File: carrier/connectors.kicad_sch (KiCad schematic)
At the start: 2 parts, among them J11 2199119-8, J12 Conn_01x05

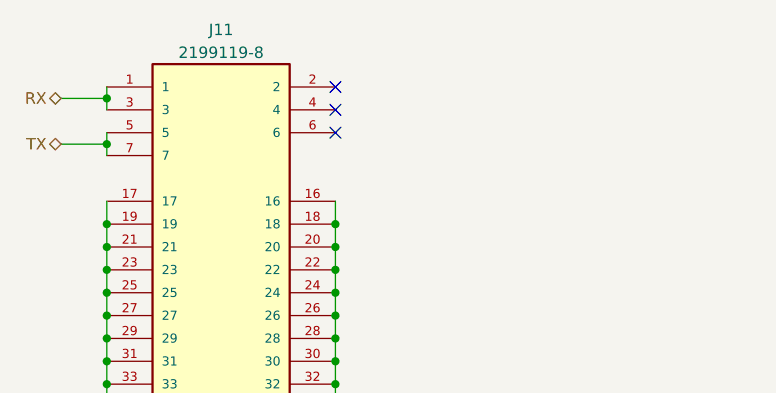
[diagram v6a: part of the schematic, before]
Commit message: Feat: most routes on i2c side and power complete
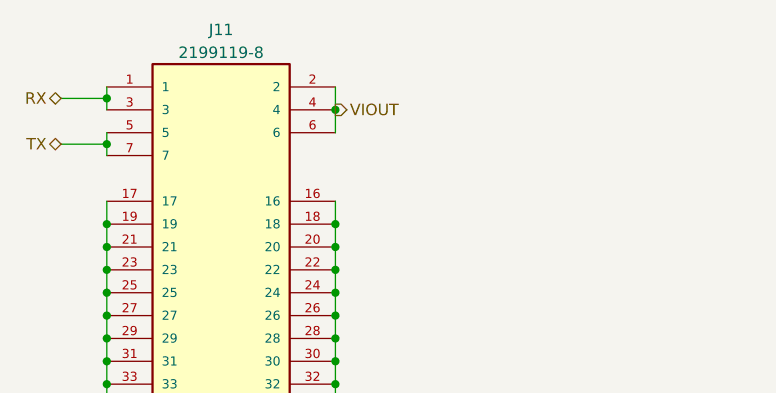
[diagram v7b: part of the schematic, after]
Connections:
- net VIOUT: now reaches J11.2
- net VIOUT: now also J11.4, J11.6
- no-connect marks 3 -> 0
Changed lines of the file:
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@@
   (junction (at 133.35 83.82) (diameter 0) (color 0 0 0 0)
   )
+  (junction (at 133.35 55.88) (diameter 0) (color 0 0 0 0)
+  )
   (junction (at 107.95 116.84) (diameter 0) (color 0 0 0 0)
   )
@@
   (junction (at 133.35 88.9) (diameter 0) (color 0 0 0 0)
   )
-  (no_connect (at 133.35 53.34))
-  (no_connect (at 133.35 55.88))
-  (no_connect (at 133.35 58.42))
   (wire (pts (xy 133.35 109.22) (xy 133.35 111.76))
     (stroke (width 0) (type default))
@@
     (stroke (width 0) (type default))
   )
+  (wire (pts (xy 133.35 55.88) (xy 133.35 58.42))
+    (stroke (width 0) (type default))
+  )
   (wire (pts (xy 107.95 88.9) (xy 107.95 91.44))
     (stroke (width 0) (type default))
@@
   )
   (wire (pts (xy 133.35 132.08) (xy 133.35 134.62))
+    (stroke (width 0) (type default))
+  )
+  (wire (pts (xy 133.35 53.34) (xy 133.35 55.88))
     (stroke (width 0) (type default))
   )
@@
     (effects (font (size 1.27 1.27)) (justify left))
   )
+  (hierarchical_label "VIOUT" (shape output) (at 133.35 55.88 0) (fields_autoplaced)
+    (effects (font (size 1.27 1.27)) (justify left))
+  )

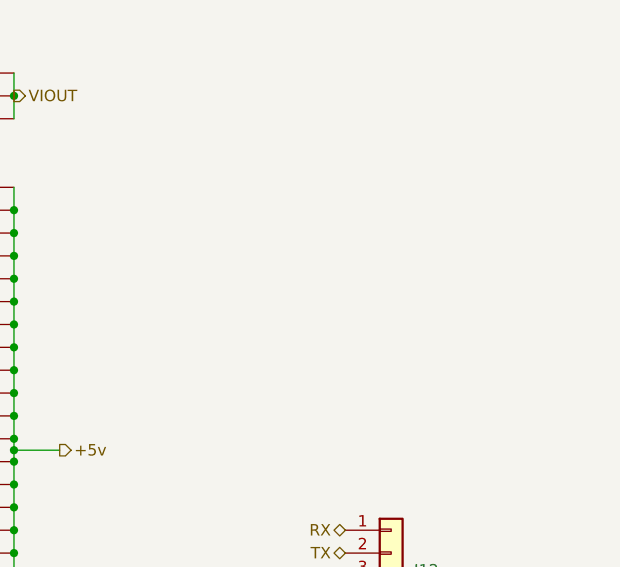
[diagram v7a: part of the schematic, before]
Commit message: Feat: all initial routes complete
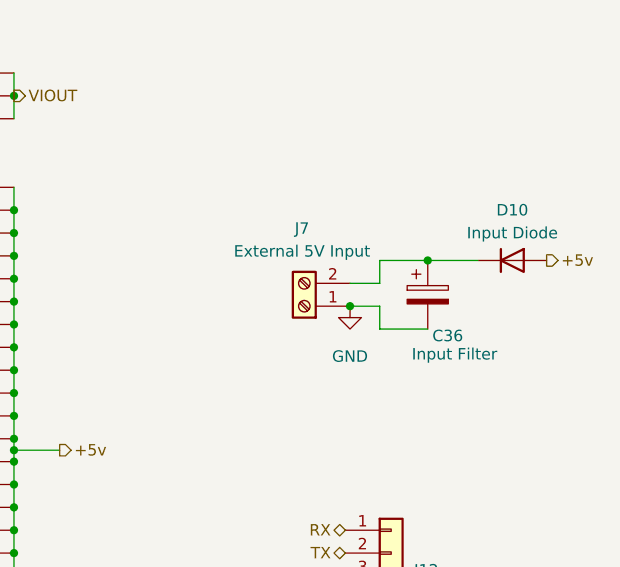
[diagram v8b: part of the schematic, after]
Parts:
- added C36: Input Filter, symbol Device:C_Polarized
- added D10: Input Diode, symbol Device:D
- added J7: External 5V Input, symbol Connector:Screw_Terminal_01x02
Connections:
- net +5v: now also D10.2 (A)
- net GND: now also C36.2, J7.1 (Pin_1)
- new net: C36.1, D10.1 (K), J7.2 (Pin_2)
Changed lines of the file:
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@@
   (junction (at 133.35 73.66) (diameter 0) (color 0 0 0 0)
   )
+  (junction (at 179.324 74.168) (diameter 0) (color 0 0 0 0)
+  )
   (junction (at 107.95 96.52) (diameter 0) (color 0 0 0 0)
   )
@@
   (junction (at 133.35 137.16) (diameter 0) (color 0 0 0 0)
   )
+  (junction (at 170.688 79.248) (diameter 0) (color 0 0 0 0)
+  )
   (junction (at 107.95 83.82) (diameter 0) (color 0 0 0 0)
   )
@@
   )
   (wire (pts (xy 133.35 121.92) (xy 133.35 124.46))
+    (stroke (width 0) (type default))
+  )
+  (wire (pts (xy 179.324 81.788) (xy 173.99 81.788))
     (stroke (width 0) (type default))
   )
@@
     (stroke (width 0) (type default))
   )
+  (wire (pts (xy 173.99 79.248) (xy 170.688 79.248))
+    (stroke (width 0) (type default))
+  )
   (wire (pts (xy 133.35 96.52) (xy 133.35 99.06))
     (stroke (width 0) (type default))
   )
+  (wire (pts (xy 179.324 74.168) (xy 173.99 74.168))
+    (stroke (width 0) (type default))
+  )
   (wire (pts (xy 107.95 137.16) (xy 107.95 139.7))
     (stroke (width 0) (type default))
@@
     (stroke (width 0) (type default))
   )
+  (wire (pts (xy 173.99 74.168) (xy 173.99 76.708))
+    (stroke (width 0) (type default))
+  )
   (wire (pts (xy 133.35 76.2) (xy 133.35 78.74))
     (stroke (width 0) (type default))
@@
   )
   (wire (pts (xy 133.35 95.25) (xy 133.35 96.52))
+    (stroke (width 0) (type default))
+  )
+  (wire (pts (xy 179.324 74.168) (xy 184.912 74.168))
     (stroke (width 0) (type default))
   )
@@
     (stroke (width 0) (type default))
   )
+  (wire (pts (xy 173.99 81.788) (xy 173.99 79.248))
+    (stroke (width 0) (type default))
+  )
   (wire (pts (xy 107.95 127) (xy 107.95 129.54))
     (stroke (width 0) (type default))
@@
   )
   (wire (pts (xy 133.35 88.9) (xy 133.35 91.44))
+    (stroke (width 0) (type default))
+  )
+  (wire (pts (xy 173.99 76.708) (xy 170.688 76.708))
     (stroke (width 0) (type default))
   )
@@
   )
   (hierarchical_label "+5v" (shape output) (at 138.43 95.25 0) (fields_autoplaced)
+    (effects (font (size 1.27 1.27)) (justify left))
+  )
+  (hierarchical_label "+5v" (shape output) (at 192.532 74.168 0) (fields_autoplaced)
     (effects (font (size 1.27 1.27)) (justify left))
   )
@@
     )
   )
+  (symbol (lib_id "Connector:Screw_Terminal_01x02") (at 165.608 79.248 180) (unit 1)
+    (in_bom yes) (on_board yes) (dnp no)
+    (property "Reference" "J7" (at 165.354 70.612 0)
+      (effects (font (size 1.27 1.27)))
+    )
+    (property "Value" "External 5V Input" (at 165.354 73.152 0)
+      (effects (font (size 1.27 1.27)))
+    )
+    (property "Footprint" "" (at 165.608 79.248 0)
+      (effects (font (size 1.27 1.27)) hide)
+    )
+    (property "Datasheet" "~" (at 165.608 79.248 0)
+      (effects (font (size 1.27 1.27)) hide)
+    )
+    (pin "1")
+    (pin "2")
+    (instances
+      (project "carrier"
+        (path "/4b1cea9d-93bc-4380-88c3-ede99bb53de2/af6c5568-d2e2-4612-83c1-6e53a7c32d99"
+          (reference "J7") (unit 1)
+        )
+      )
+    )
+  )
   (symbol (lib_id "power:GND") (at 163.83 114.3 0) (unit 1)
     (in_bom yes) (on_board yes) (dnp no)
@@
     )
   )
+  (symbol (lib_id "power:GND") (at 170.688 79.248 0) (unit 1)
+    (in_bom yes) (on_board yes) (dnp no) (fields_autoplaced)
+    (property "Reference" "#PWR037" (at 170.688 85.598 0)
+      (effects (font (size 1.27 1.27)) hide)
+    )
+    (property "Value" "GND" (at 170.688 84.836 0)
+      (effects (font (size 1.27 1.27)))
+    )
+    (property "Footprint" "" (at 170.688 79.248 0)
+      (effects (font (size 1.27 1.27)) hide)
+    )
+    (property "Datasheet" "" (at 170.688 79.248 0)
+      (effects (font (size 1.27 1.27)) hide)
+    )
+    (pin "1")
+    (instances
+      (project "carrier"
+        (path "/4b1cea9d-93bc-4380-88c3-ede99bb53de2/af6c5568-d2e2-4612-83c1-6e53a7c32d99"
+          (reference "#PWR037") (unit 1)
+        )
+      )
+    )
+  )
   (symbol (lib_id "power:GND") (at 107.95 143.51 0) (unit 1)
     (in_bom yes) (on_board yes) (dnp no) (fields_autoplaced)
@@
         )
       )
+    )
+  )
+  (symbol (lib_id "Device:D") (at 188.722 74.168 0) (unit 1)
+    (in_bom yes) (on_board yes) (dnp no) (fields_autoplaced)
+    (property "Reference" "D10" (at 188.722 68.58 0)
+      (effects (font (size 1.27 1.27)))
+    )
+    (property "Value" "Input Diode" (at 188.722 71.12 0)
+      (effects (font (size 1.27 1.27)))
+    )
+    (property "Footprint" "" (at 188.722 74.168 0)
+      (effects (font (size 1.27 1.27)) hide)
+    )
+    (property "Datasheet" "~" (at 188.722 74.168 0)
+      (effects (font (size 1.27 1.27)) hide)
+    )
+    (property "Sim.Device" "D" (at 188.722 74.168 0)
+      (effects (font (size 1.27 1.27)) hide)
+    )
+    (property "Sim.Pins" "1=K 2=A" (at 188.722 74.168 0)
+      (effects (font (size 1.27 1.27)) hide)
+    )
+    (pin "1")
+    (pin "2")
+    (instances
+      (project "carrier"
+        (path "/4b1cea9d-93bc-4380-88c3-ede99bb53de2/af6c5568-d2e2-4612-83c1-6e53a7c32d99"
+          (reference "D10") (unit 1)
+        )
+      )
+    )
+  )
+  (symbol (lib_id "Device:C_Polarized") (at 179.324 77.978 0) (unit 1)
+    (in_bom yes) (on_board yes) (dnp no)
+    (property "Reference" "C36" (at 179.832 82.55 0)
+      (effects (font (size 1.27 1.27)) (justify left))
+    )
+    (property "Value" "Input Filter" (at 177.546 84.582 0)
+      (effects (font (size 1.27 1.27)) (justify left))
+    )
+    (property "Footprint" "" (at 180.2892 81.788 0)
+      (effects (font (size 1.27 1.27)) hide)
+    )
+    (property "Datasheet" "~" (at 179.324 77.978 0)
+      (effects (font (size 1.27 1.27)) hide)
+    )
+    (pin "1")
+    (pin "2")
+    (instances
+      (project "carrier"
+        (path "/4b1cea9d-93bc-4380-88c3-ede99bb53de2/af6c5568-d2e2-4612-83c1-6e53a7c32d99"
+          (reference "C36") (unit 1)
+        )
+      )
